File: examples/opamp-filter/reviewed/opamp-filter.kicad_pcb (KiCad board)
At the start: 2 copper layers, 58 x 42 mm, 22 parts, among them J1 IN, J2 5V, J3 OUT, U1 MCP6001R, U2 MCP6001R

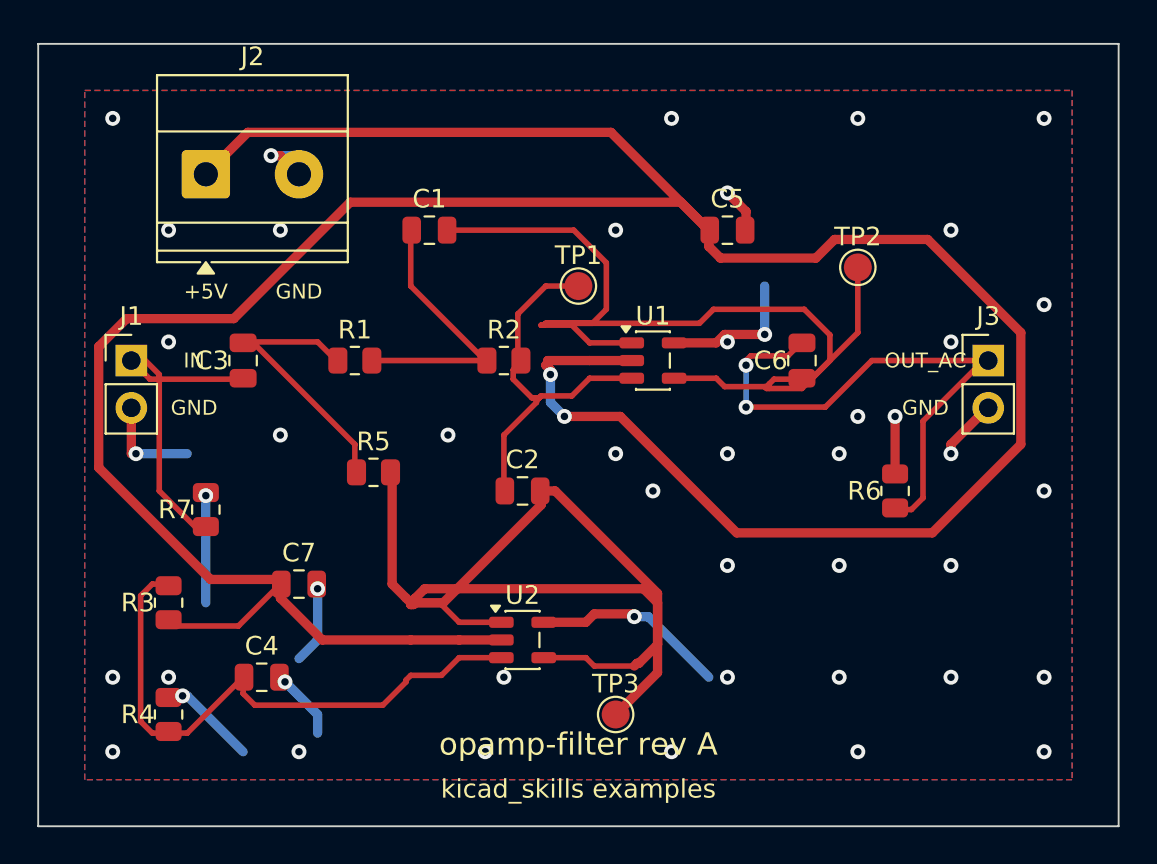
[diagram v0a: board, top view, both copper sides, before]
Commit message: Put the silkscreen where the board is not
Three legends were printed across pads. The board id was written at the
bottom centre whether or not the bottom centre was a module; the pin
names beside a connector went toward the middle of the board, which on a
carrier is the module they are labelling; and a footprint's designator
stayed where its library had drawn it, which on a part with pads down
both sides and along the bottom is the middle of a pad. Silk over a pad
is not a legend - the mask opens there, the ink comes off in
fabrication, and what is left is a pad that will not wet.

So all three ask first. The board id offers its usual spot and then the
next-best strips in turn. A pin name measures the *area* it would take
from other footprints on either side of the row and picks the smaller,
which chooses outboard on its own where there is an edge to face, and
matters because "half a legend over a module's pads" and "a tenth of a
millimetre into a chip capacitor's courtyard" are both one collision and
only one of them is a defect. A designator steps to the first spot in
its own footprint that no pad occupies.

Modules that draw no courtyard are measured by their pads instead:
taking a missing courtyard to mean the part occupies no board is how the
Pico's legend ended up across it.

The Pico carrier also grew: its two headers and the module run the
length of the board, and the plane could not get past their pin rows at
either end, so it was three islands with the return current going the
long way round. Six millimetres of board below the last pin is what a
plane needs to be one plane.
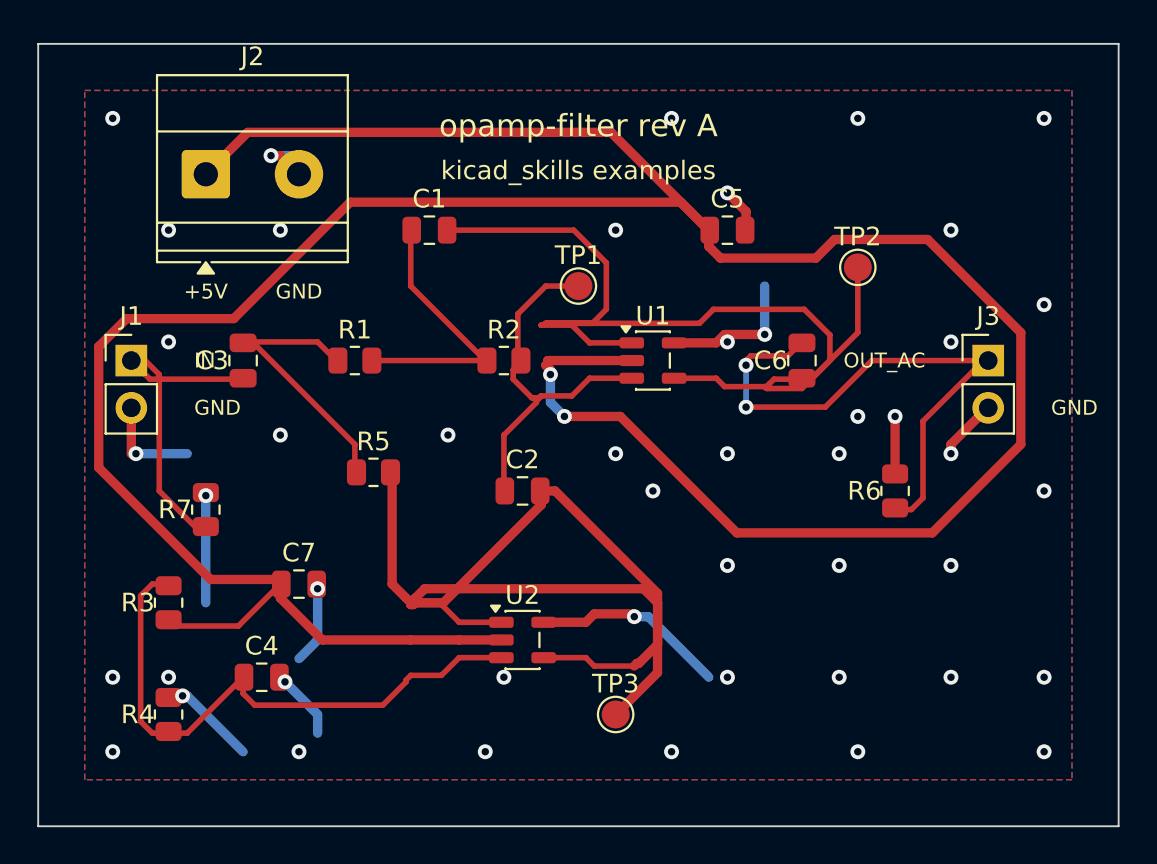
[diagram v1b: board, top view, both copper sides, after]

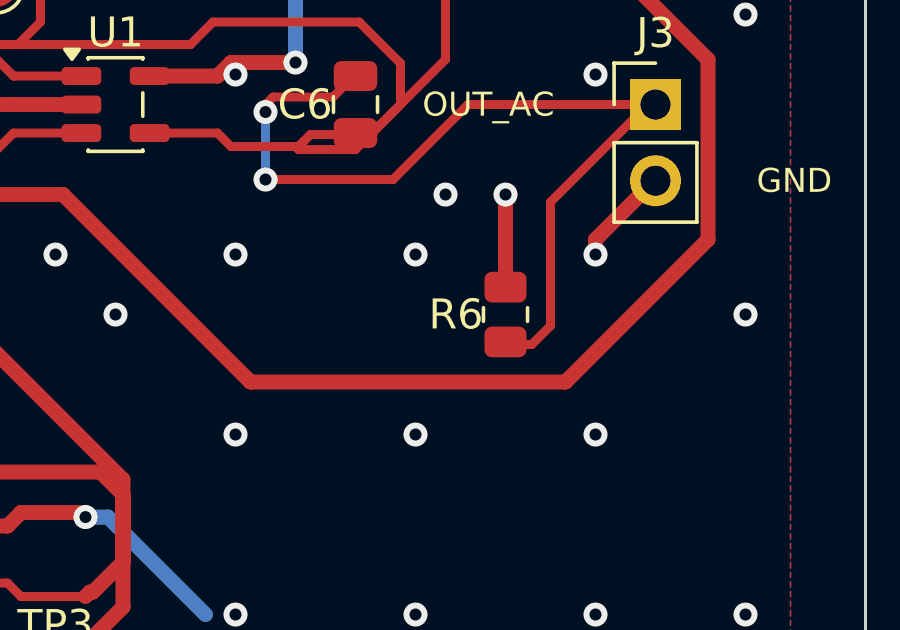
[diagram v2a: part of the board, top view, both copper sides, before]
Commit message: Give a turned part's designator somewhere to go
A designator prints horizontally whatever the footprint's rotation, so
on a part turned 90 degrees the string reaches along the axis the
footprint's own frame calls the other one - and a two-terminal chip part
is narrower than its own three-character name. Every spot inside the
footprint touched a pad, and the search gave up and left it there.

It now looks along both local axes, at increasing distance, starting
from half the string plus half the part. Near still beats far.

The fold-back pass also stops refusing to unfold a run that walks back
past where it set out from. That refusal was there because deleting the
point moves the corner before it; usually that corner is the other half
of the same fold and both go. Now it checks: if what is left is 90
degrees or wider, unfold; if not, the run keeps its spur rather than
trade it for a worse bend.
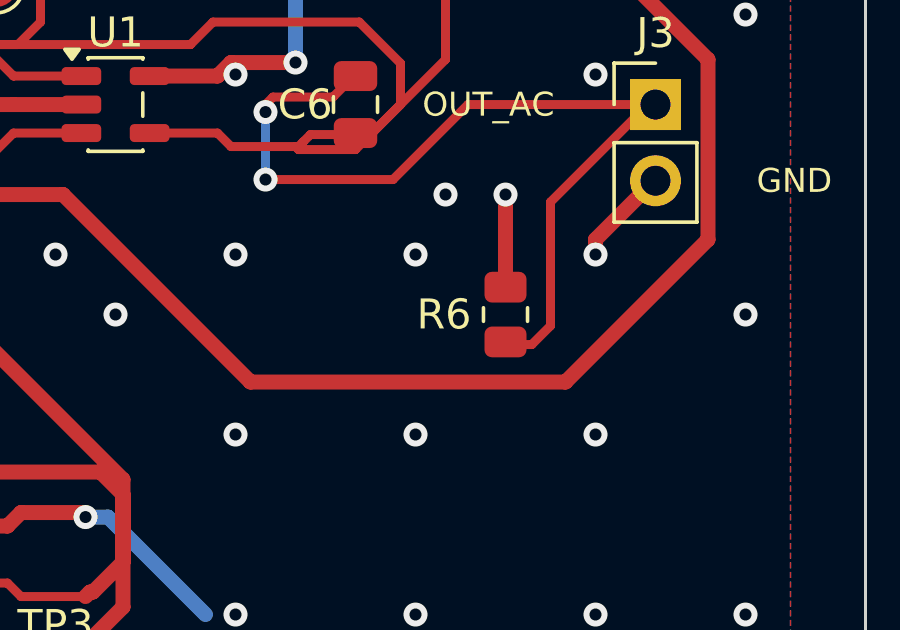
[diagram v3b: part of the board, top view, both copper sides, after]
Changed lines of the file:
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@@
     (tags "resistor")
     (property "Reference" "R6"
-      (at 0 -1.65 0)
+      (at 0.0 -2.05 0)
       (layer "F.SilkS")
       (effects
@@
     )
     (property "Tolerance" "1%"
-      (at 0 -1.65 0)
+      (at 0.0 -2.05 0)
       (layer "F.Fab")
       (hide yes)
@@
     )
     (property "Power" "0.125W"
-      (at 0 -1.65 0)
+      (at 0.0 -2.05 0)
       (layer "F.Fab")
       (hide yes)
@@
     )
     (property "MPN" "RC0805FR-07100KL"
-      (at 0 -1.65 0)
+      (at 0.0 -2.05 0)
       (layer "F.Fab")
       (hide yes)
@@
     )
     (property "Manufacturer" "Yageo"
-      (at 0 -1.65 0)
+      (at 0.0 -2.05 0)
       (layer "F.Fab")
       (hide yes)
@@
     )
     (property "Datasheet" "https://www.yageo.com/upload/media/product/productsearch/datasheet/rchip/PYu-RC_Group_51_RoHS_L_12.pdf"
-      (at 0 -1.65 0)
+      (at 0.0 -2.05 0)
       (layer "F.Fab")
       (hide yes)
